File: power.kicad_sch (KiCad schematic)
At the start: 47 parts, among them J4 Conn_01x02, U3 TLV75733PDBV, U4 TPS56A37, U5 TPS56A37

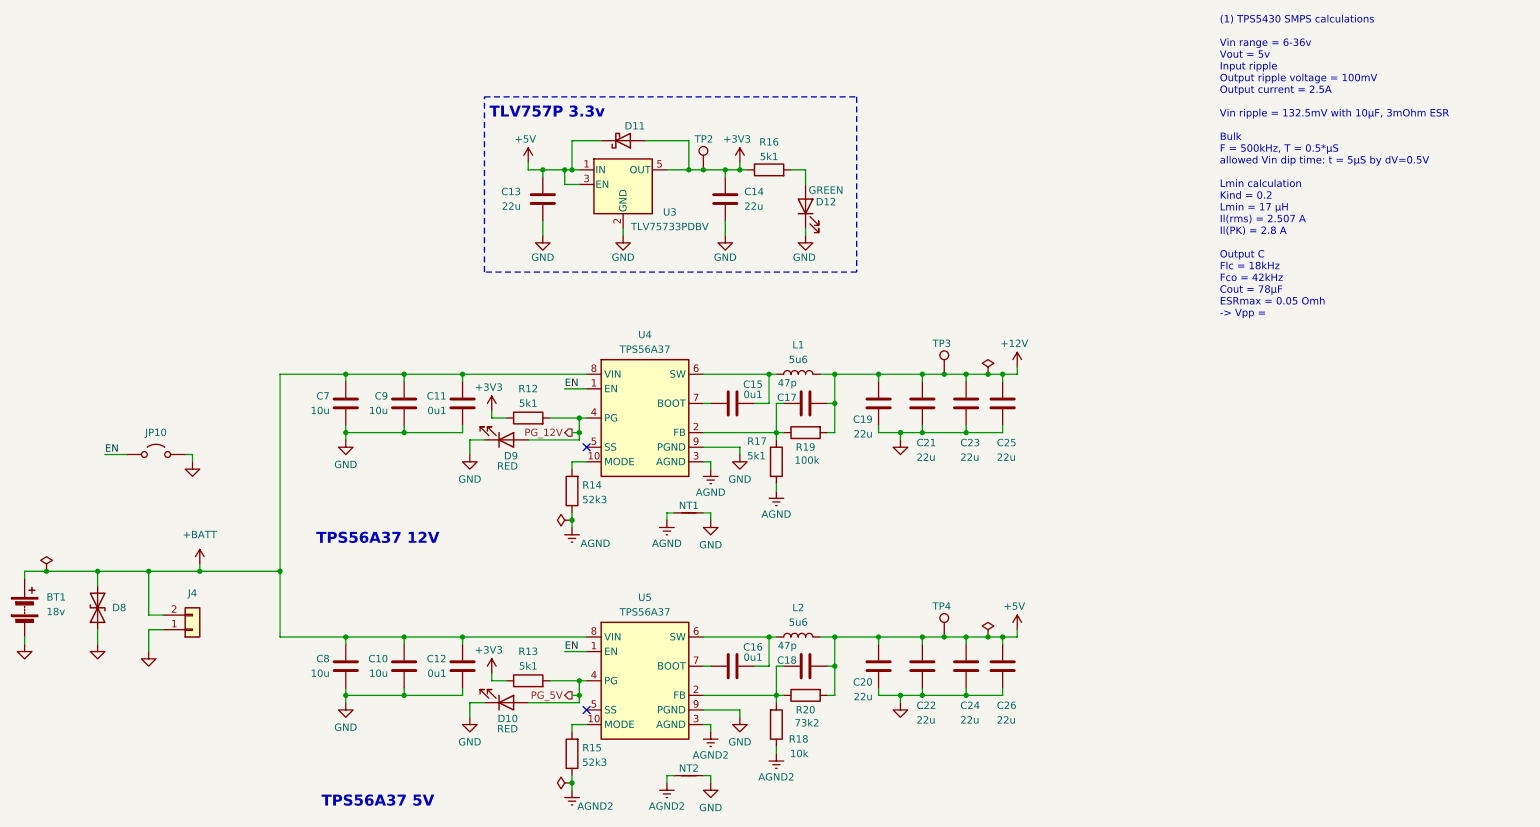
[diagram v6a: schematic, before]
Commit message: schem/pcb: prevent TPS56A37 reverse current with new oringed 5v mcu rail
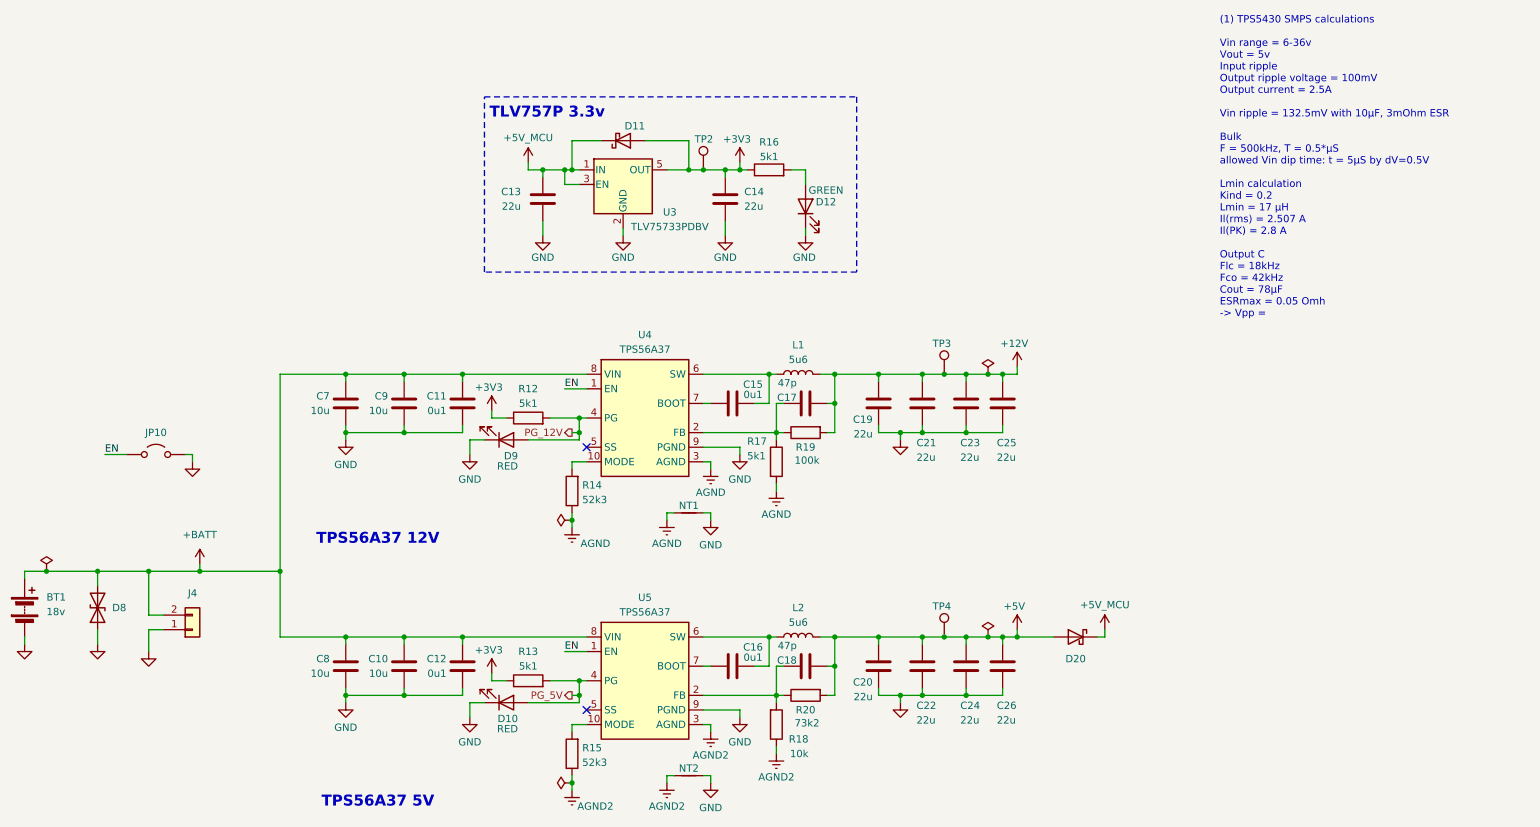
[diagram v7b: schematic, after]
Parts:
- added D20: D_Schottky, Diode_SMD:D_SMA, symbol Device:D_Schottky
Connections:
- net +5V: now also D20.2 (A); no longer C13.2, D11.1 (K), U3.1 (IN), U3.3 (EN)
- new net +5V_MCU: C13.2, D11.1 (K), D20.1 (K), U3.1 (IN), U3.3 (EN)
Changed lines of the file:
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@@
 	)
 	(junction
+		(at 199.39 123.19)
+		(diameter 0)
+		(color 0 0 0 0)
+	)
+	(junction
 		(at 194.31 77.47)
 		(diameter 0)
@@
 	(wire
 		(pts
+			(xy 214.63 123.19) (xy 213.36 123.19)
+		)
+		(stroke
+			(width 0)
+			(type default)
+		)
+	)
+	(wire
+		(pts
 			(xy 142.24 41.91) (xy 144.78 41.91)
 		)
@@
 	(wire
 		(pts
+			(xy 199.39 123.19) (xy 205.74 123.19)
+		)
+		(stroke
+			(width 0)
+			(type default)
+		)
+	)
+	(wire
+		(pts
 			(xy 71.12 123.19) (xy 82.55 123.19)
 		)
@@
 	(wire
 		(pts
+			(xy 214.63 121.92) (xy 214.63 123.19)
+		)
+		(stroke
+			(width 0)
+			(type default)
+		)
+	)
+	(wire
+		(pts
 			(xy 57.15 111.76) (xy 71.12 111.76)
 		)
@@
 	)
 	(symbol
-		(lib_id "power:+12V")
-		(at 114.3 40.64 0)
-		(unit 1)
-		(exclude_from_sim no)
-		(in_bom yes)
-		(on_board yes)
-		(dnp no)
-		(property "Reference" "#PWR036"
-			(at 114.3 44.45 0)
-			(effects
-				(font
-					(size 1.27 1.27)
-				)
-				(hide yes)
-			)
-		)
-		(property "Value" "+5V"
-			(at 113.792 36.576 0)
-			(effects
-				(font
-					(size 1.27 1.27)
-				)
-			)
-		)
-		(property "Footprint" ""
-			(at 114.3 40.64 0)
-			(effects
-				(font
-					(size 1.27 1.27)
-				)
-				(hide yes)
-			)
-		)
-		(property "Datasheet" ""
-			(at 114.3 40.64 0)
-			(effects
-				(font
-					(size 1.27 1.27)
-				)
-				(hide yes)
-			)
-		)
-		(property "Description" "Power symbol creates a global label with name \"+12V\""
-			(at 114.3 40.64 0)
-			(effects
-				(font
-					(size 1.27 1.27)
-				)
-				(hide yes)
-			)
-		)
-		(pin "1"
-		)
-		(instances
-			(project "valrob-carte-alim-cdf-1"
-				(path "/8d7b287d-627f-46aa-8c27-0b5ed29ab4a2/0cc01053-a223-4e8e-b0aa-a1ec618db290"
-					(reference "#PWR036")
-					(unit 1)
-				)
-			)
-		)
-	)
-	(symbol
 		(lib_id "power:GNDREF")
 		(at 138.43 148.59 0)
@@
 	)
 	(symbol
+		(lib_id "power:+5V")
+		(at 114.3 40.64 0)
+		(mirror y)
+		(unit 1)
+		(exclude_from_sim no)
+		(in_bom yes)
+		(on_board yes)
+		(dnp no)
+		(property "Reference" "#PWR036"
+			(at 114.3 44.45 0)
+			(effects
+				(font
+					(size 1.27 1.27)
+				)
+				(hide yes)
+			)
+		)
+		(property "Value" "+5V_MCU"
+			(at 114.3 36.322 0)
+			(effects
+				(font
+					(size 1.27 1.27)
+				)
+			)
+		)
+		(property "Footprint" ""
+			(at 114.3 40.64 0)
+			(effects
+				(font
+					(size 1.27 1.27)
+				)
+				(hide yes)
+			)
+		)
+		(property "Datasheet" ""
+			(at 114.3 40.64 0)
+			(effects
+				(font
+					(size 1.27 1.27)
+				)
+				(hide yes)
+			)
+		)
+		(property "Description" "Power symbol creates a global label with name \"+5V\""
+			(at 114.3 40.64 0)
+			(effects
+				(font
+					(size 1.27 1.27)
+				)
+				(hide yes)
+			)
+		)
+		(pin "1"
+		)
+		(instances
+			(project "valrob-carte-alim-cdf-1"
+				(path "/8d7b287d-627f-46aa-8c27-0b5ed29ab4a2/0cc01053-a223-4e8e-b0aa-a1ec618db290"
+					(reference "#PWR036")
+					(unit 1)
+				)
+			)
+		)
+	)
+	(symbol
 		(lib_id "Connector:TestPoint")
 		(at 186.69 123.19 0)
@@
 	)
 	(symbol
+		(lib_id "power:+5V")
+		(at 214.63 121.92 0)
+		(mirror y)
+		(unit 1)
+		(exclude_from_sim no)
+		(in_bom yes)
+		(on_board yes)
+		(dnp no)
+		(property "Reference" "#PWR083"
+			(at 214.63 125.73 0)
+			(effects
+				(font
+					(size 1.27 1.27)
+				)
+				(hide yes)
+			)
+		)
+		(property "Value" "+5V_MCU"
+			(at 214.63 117.602 0)
+			(effects
+				(font
+					(size 1.27 1.27)
+				)
+			)
+		)
+		(property "Footprint" ""
+			(at 214.63 121.92 0)
+			(effects
+				(font
+					(size 1.27 1.27)
+				)
+				(hide yes)
+			)
+		)
+		(property "Datasheet" ""
+			(at 214.63 121.92 0)
+			(effects
+				(font
+					(size 1.27 1.27)
+				)
+				(hide yes)
+			)
+		)
+		(property "Description" "Power symbol creates a global label with name \"+5V\""
+			(at 214.63 121.92 0)
+			(effects
+				(font
+					(size 1.27 1.27)
+				)
+				(hide yes)
+			)
+		)
+		(pin "1"
+		)
+		(instances
+			(project "valrob-carte-alim-cdf-1"
+				(path "/8d7b287d-627f-46aa-8c27-0b5ed29ab4a2/0cc01053-a223-4e8e-b0aa-a1ec618db290"
+					(reference "#PWR083")
+					(unit 1)
+				)
+			)
+		)
+	)
+	(symbol
 		(lib_id "GLCS:TPS56A37")
 		(at 134.62 80.01 0)
@@
 					(unit 1)
 				)
+			)
+		)
+	)
+	(symbol
+		(lib_id "Device:D_Schottky")
+		(at 209.55 123.19 0)
+		(mirror y)
+		(unit 1)
+		(exclude_from_sim no)
+		(in_bom yes)
+		(on_board yes)
+		(dnp no)
+		(property "Reference" "D20"
+			(at 209.55 127 0)
+			(effects
+				(font
+					(size 1.27 1.27)
+				)
+			)
+		)
+		(property "Value" "D_Schottky"
+			(at 209.8675 119.38 0)
+			(effects
+				(font
+					(size 1.27 1.27)
+				)
+				(hide yes)
+			)
+		)
+		(property "Footprint" "Diode_SMD:D_SMA"
+			(at 209.55 123.19 0)
+			(effects
+				(font
+					(size 1.27 1.27)
+				)
+				(hide yes)
+			)
+		)
+		(property "Datasheet" "~"
+			(at 209.55 123.19 0)
+			(effects
+				(font
+					(size 1.27 1.27)
+				)
+				(hide yes)
+			)
+		)
+		(property "Description" "Schottky diode"
+			(at 209.55 123.19 0)
+			(effects
+				(font
+					(size 1.27 1.27)
+				)
+				(hide yes)
+			)
+		)
+		(property "Manufacturer" "Microdiode Semiconductor (MDD)"
+			(at 209.55 123.19 0)
+			(effects
+				(font
+					(size 1.27 1.27)
+				)
+				(hide yes)
+			)
+		)
+		(property "Manufacturer Part Number" "SS54"
+			(at 209.55 123.19 0)
+			(effects
+				(font
+					(size 1.27 1.27)
+				)
+				(hide yes)
+			)
+		)
+		(property "Basic" "Y"
+			(at 209.55 123.19 0)
+			(effects
+				(font
+					(size 1.27 1.27)
+				)
+				(hide yes)
+			)
+		)
+		(property "JLCPCB Part #" "C22452"
+			(at 209.55 123.19 0)
+			(effects
+				(font
+					(size 1.27 1.27)
+				)
+				(hide yes)
+			)
+		)
+		(pin "2"
+		)
+		(pin "1"
+		)
+		(instances
+			(project "valrob-carte-alim-cdf-1"
+				(path "/8d7b287d-627f-46aa-8c27-0b5ed29ab4a2/0cc01053-a223-4e8e-b0aa-a1ec618db290"
+					(reference "D20")
+					(unit 1)
+				)

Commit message: schem/pcb: update batt connector and efuses footprints
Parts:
- J4: footprint TerminalBlock_Phoenix:TerminalBlock_Phoenix_MKDS-1,5-2-5.08_1x02_P5.08mm_Horizontal -> Connector_JST:JST_XH_B2B-XH-A_1x02_P2.50mm_Vertical
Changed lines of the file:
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@@
 	)
 	(symbol
+		(lib_id "Connector_Generic:Conn_01x02")
+		(at 55.88 121.92 0)
+		(mirror x)
+		(unit 1)
+		(exclude_from_sim no)
+		(in_bom yes)
+		(on_board yes)
+		(dnp no)
+		(fields_autoplaced yes)
+		(property "Reference" "J4"
+			(at 55.88 115.57 0)
+			(effects
+				(font
+					(size 1.27 1.27)
+				)
+			)
+		)
+		(property "Value" "Conn_01x02"
+			(at 58.42 119.3801 0)
+			(effects
+				(font
+					(size 1.27 1.27)
+				)
+				(justify left)
+				(hide yes)
+			)
+		)
+		(property "Footprint" "Connector_JST:JST_XH_B2B-XH-A_1x02_P2.50mm_Vertical"
+			(at 55.88 121.92 0)
+			(effects
+				(font
+					(size 1.27 1.27)
+				)
+				(hide yes)
+			)
+		)
+		(property "Datasheet" "~"
+			(at 55.88 121.92 0)
+			(effects
+				(font
+					(size 1.27 1.27)
+				)
+				(hide yes)
+			)
+		)
+		(property "Description" "Generic connector, single row, 01x02, script generated (kicad-library-utils/schlib/autogen/connector/)"
+			(at 55.88 121.92 0)
+			(effects
+				(font
+					(size 1.27 1.27)
+				)
+				(hide yes)
+			)
+		)
+		(property "Basic" "Z"
+			(at 55.88 121.92 0)
+			(effects
+				(font
+					(size 1.27 1.27)
+				)
+				(hide yes)
+			)
+		)
+		(property "JLCPCB Part #" "C158012"
+			(at 55.88 121.92 0)
+			(effects
+				(font
+					(size 1.27 1.27)
+				)
+				(hide yes)
+			)
+		)
+		(property "Manufacturer" "JST"
+			(at 55.88 121.92 0)
+			(effects
+				(font
+					(size 1.27 1.27)
+				)
+				(hide yes)
+			)
+		)
+		(property "Manufacturer Part Number" "B2B-XH-A(LF)(SN)"
+			(at 55.88 121.92 0)
+			(effects
+				(font
+					(size 1.27 1.27)
+				)
+				(hide yes)
+			)
+		)
+		(pin "2"
+		)
+		(pin "1"
+		)
+		(instances
+			(project "valrob-carte-alim-cdf-1"
+				(path "/8d7b287d-627f-46aa-8c27-0b5ed29ab4a2/0cc01053-a223-4e8e-b0aa-a1ec618db290"
+					(reference "J4")
+					(unit 1)
+				)
+			)
+		)
+	)
+	(symbol
 		(lib_id "power:GND")
 		(at 104.14 137.16 0)
@@
 					(unit 1)
 				)
-			)
-		)
-	)
-	(symbol
-		(lib_id "Connector_Generic:Conn_01x02")
-		(at 55.88 121.92 0)
-		(mirror x)
-		(unit 1)
-		(exclude_from_sim no)
-		(in_bom yes)
-		(on_board yes)
-		(dnp no)
-		(fields_autoplaced yes)
-		(property "Reference" "J4"
-			(at 55.88 115.57 0)
-			(effects
-				(font
-					(size 1.27 1.27)
-				)
-			)
-		)
-		(property "Value" "Conn_01x02"
-			(at 58.42 119.3801 0)
-			(effects
-				(font
-					(size 1.27 1.27)
-				)
-				(justify left)
-				(hide yes)
-			)
-		)
-		(property "Footprint" "TerminalBlock_Phoenix:TerminalBlock_Phoenix_MKDS-1,5-2-5.08_1x02_P5.08mm_Horizontal"
-			(at 55.88 121.92 0)
-			(effects
-				(font
-					(size 1.27 1.27)
-				)
-				(hide yes)
-			)
-		)
-		(property "Datasheet" "~"
-			(at 55.88 121.92 0)
-			(effects
-				(font
-					(size 1.27 1.27)
-				)
-				(hide yes)
-			)
-		)
-		(property "Description" "Generic connector, single row, 01x02, script generated (kicad-library-utils/schlib/autogen/connector/)"
-			(at 55.88 121.92 0)
-			(effects
-				(font
-					(size 1.27 1.27)
-				)
-				(hide yes)
-			)
-		)
-		(property "Basic" "Z"
-			(at 55.88 121.92 0)
-			(effects
-				(font
-					(size 1.27 1.27)
-				)
-				(hide yes)
-			)
-		)
-		(property "JLCPCB Part #" "C158012"
-			(at 55.88 121.92 0)
-			(effects
-				(font
-					(size 1.27 1.27)
-				)
-				(hide yes)
-			)
-		)
-		(property "Manufacturer" "JST"
-			(at 55.88 121.92 0)
-			(effects
-				(font
-					(size 1.27 1.27)
-				)
-				(hide yes)
-			)
-		)
-		(property "Manufacturer Part Number" "B2B-XH-A(LF)(SN)"
-			(at 55.88 121.92 0)
-			(effects
-				(font
-					(size 1.27 1.27)
-				)
-				(hide yes)
-			)
-		)
-		(pin "2"
-		)
-		(pin "1"
-		)
-		(instances
-			(project "valrob-carte-alim-cdf-1"
-				(path "/8d7b287d-627f-46aa-8c27-0b5ed29ab4a2/0cc01053-a223-4e8e-b0aa-a1ec618db290"
-					(reference "J4")
-					(unit 1)
-				)
